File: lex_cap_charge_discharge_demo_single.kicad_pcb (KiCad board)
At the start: 2 copper layers, 38 x 33.5 mm, 8 parts, among them J1 +5V, J2 GND, SW1 charge, SW2 discharge

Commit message: Tweak R vals
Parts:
- R1: value 400K -> 10K
- R2: value 470 -> 330
- moved R1 79.5 mm to (53.0, 59.5), turned to -90 degrees
- moved R2 77.1 mm to (65.9, 53.0)
- moved SW1 73.8 mm to (52.9, 75.0)
- moved J1 70.8 mm to (53.0, 53.0)
- moved SW2 70.2 mm to (76.4, 75.0)
- moved J2 69.9 mm to (57.0, 53.0)
- moved D1 66.4 mm to (74.0, 64.0)
- moved C1 63.9 mm to (64.0, 64.0)
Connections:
- C1 pad 1: Net-(SW1-A) -> Net-(SW1-B)
- C1 pad 2: Net-(C1-Pad2) -> GND
- R1 pad 1: Net-(C1-Pad2) -> +5V
- R1 pad 2: GND -> Net-(SW1-A)
- SW1 pad 2: +5V -> Net-(SW1-B)
- SW2 pad 2: Net-(SW1-A) -> Net-(SW1-B)
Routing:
- net Net-(SW1-B): track 0.00 -> 32.0 mm
- net Net-(D1-A): track 41.2 -> 11.0 mm
- net +5V: track 28.8 -> 6.50 mm
- net Net-(D1-K): track 29.2 -> 11.2 mm
- net Net-(SW1-A): track 25.4 -> 7.93 mm
- net GND: track 30.8 -> 20.0 mm
- net Net-(C1-Pad2): track 4.88 -> 0.00 mm

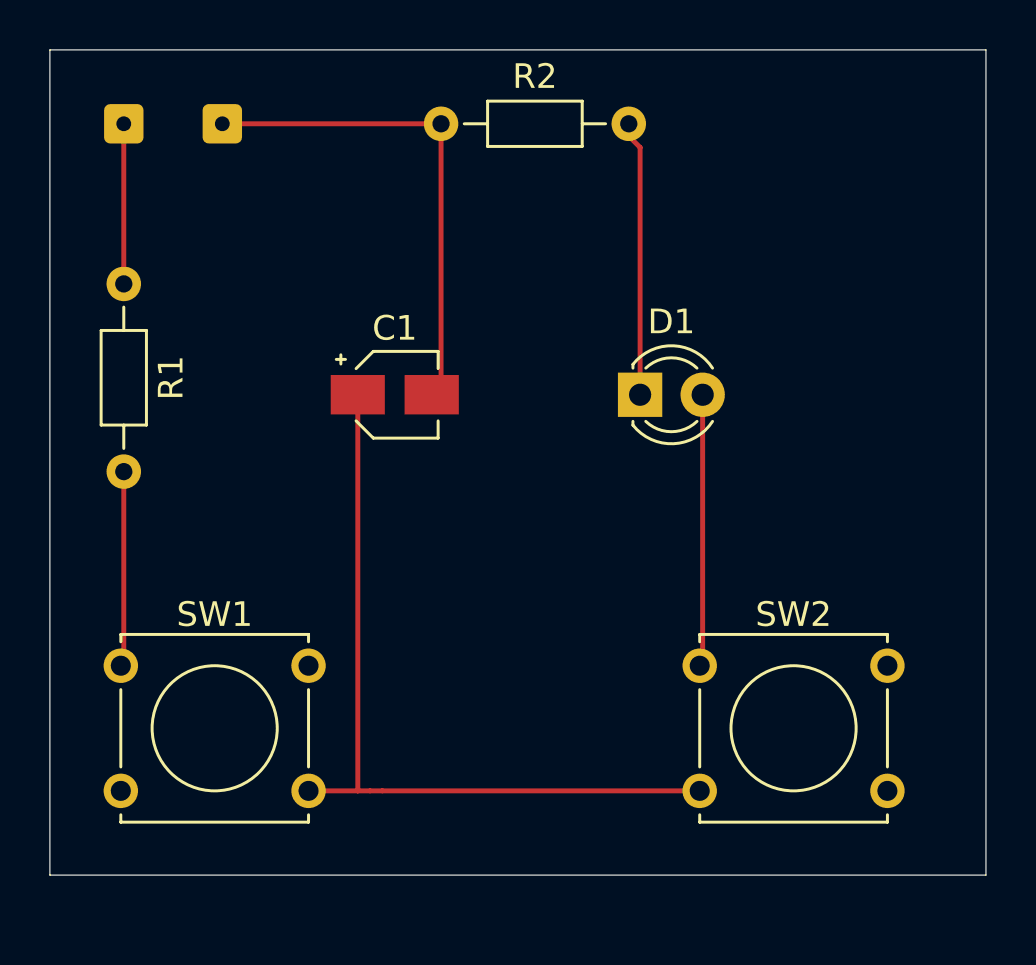
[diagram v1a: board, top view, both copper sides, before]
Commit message: Change various incl +V, GND solder pads; move components to  0.24mm standard pitch grid; add text front/back
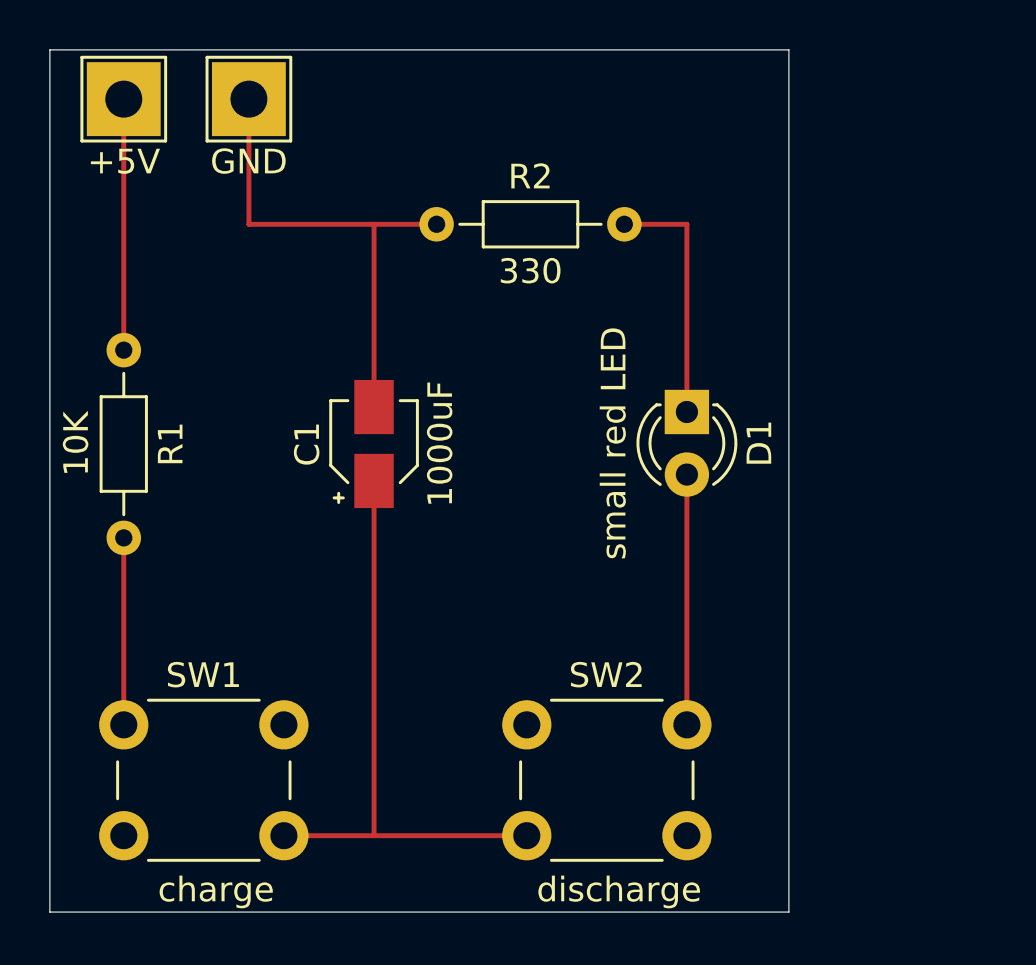
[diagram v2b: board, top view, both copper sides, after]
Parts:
- D1: value LED -> small red LED
- J1, J2: footprint Connector_Wire:SolderWire-0.1sqmm_1x01_D0.4mm_OD1mm -> TestPoint:TestPoint_THTPad_3.0x3.0mm_Drill1.5mm
- SW1, SW2: footprint Button_Switch_THT:SW_Tactile_Straight_KSL0Axx1LFTR -> Button_Switch_THT:SW_PUSH_6mm_H4.3mm
- moved SW2 7.42 mm to (69.4, 77.4)
- moved R2 4.08 mm to (65.7, 57.1)
- moved R1 2.69 mm to (53.0, 62.2)
- moved SW1 2.40 mm to (53.0, 77.4)
- moved C1 2.17 mm to (63.2, 66.0), turned to 90 degrees
- moved D1 2.02 mm to (75.9, 64.7), turned to -90 degrees
- moved J2 1.47 mm to (58.1, 52.0)
- moved J1 1.00 mm to (53.0, 52.0)
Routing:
- net Net-(SW1-B): track 32.0 -> 24.3 mm
- net +5V: track 6.50 -> 10.2 mm
- net Net-(D1-K): track 11.2 -> 10.2 mm
- net Net-(D1-A): track 11.0 -> 10.2 mm
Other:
- board size 38 x 33.5 mm -> 30 x 35 mm

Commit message: Put track across connected switch pins:
to keep kiCad ERC happy. Also more forgiving of a switch pin joint failure.
Apparently if I just ignored the warning it would be fine too.
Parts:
- J1, J2: footprint TestPoint:TestPoint_THTPad_3.0x3.0mm_Drill1.5mm -> TestPoint:TestPoint_THTPad_2.0x2.0mm_Drill1.0mm
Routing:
- net Net-(SW1-B): track 24.3 -> 37.3 mm
- net Net-(SW1-A): track 7.59 -> 14.1 mm
- net Net-(D1-A): track 10.2 -> 16.7 mm
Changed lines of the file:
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@@
 		)
 	)
-	(footprint "TestPoint:TestPoint_THTPad_3.0x3.0mm_Drill1.5mm"
+	(footprint "TestPoint:TestPoint_THTPad_2.0x2.0mm_Drill1.0mm"
 		(layer "F.Cu")
 		(at 53 52)
-		(descr "THT rectangular pad as test Point, square 3.0mm side length, hole diameter 1.5mm")
+		(descr "THT rectangular pad as test Point, square 2.0mm_Drill1.0mm  side length, hole diameter 1.0mm")
 		(tags "test point THT pad rectangle square")
 		(property "Reference" "J1"
-			(at 0 -2.398 0)
+			(at 0 -1.998 0)
 			(layer "User.1")
 			(effects
@@
 		)
 		(property "Value" "+5V"
-			(at 0 2.55 0)
+			(at 0 2.05 0)
 			(layer "F.SilkS")
 			(effects
@@
 		(attr exclude_from_pos_files)
 		(fp_line
-			(start -1.7 -1.7)
-			(end 1.7 -1.7)
-			(stroke
-				(width 0.12)
-				(type solid)
-			)
-			(layer "F.SilkS")
-		)
-		(fp_line
-			(start -1.7 1.7)
-			(end -1.7 -1.7)
-			(stroke
-				(width 0.12)
-				(type solid)
-			)
-			(layer "F.SilkS")
-		)
-		(fp_line
-			(start 1.7 -1.7)
-			(end 1.7 1.7)
-			(stroke
-				(width 0.12)
-				(type solid)
-			)
-			(layer "F.SilkS")
-		)
-		(fp_line
-			(start 1.7 1.7)
-			(end -1.7 1.7)
-			(stroke
-				(width 0.12)
-				(type solid)
-			)
-			(layer "F.SilkS")
-		)
-		(fp_line
-			(start -2 -2)
-			(end -2 2)
-			(stroke
-				(width 0.05)
-				(type solid)
-			)
-			(layer "F.CrtYd")
-		)
-		(fp_line
-			(start -2 -2)
-			(end 2 -2)
-			(stroke
-				(width 0.05)
-				(type solid)
-			)
-			(layer "F.CrtYd")
-		)
-		(fp_line
-			(start 2 2)
-			(end -2 2)
-			(stroke
-				(width 0.05)
-				(type solid)
-			)
-			(layer "F.CrtYd")
-		)
-		(fp_line
-			(start 2 2)
-			(end 2 -2)
-			(stroke
-				(width 0.05)
-				(type solid)
-			)
-			(layer "F.CrtYd")
+			(start -1.2 -1.2)
+			(end 1.2 -1.2)
+			(stroke
+				(width 0.12)
+				(type solid)
+			)
+			(layer "F.SilkS")
+		)
+		(fp_line
+			(start -1.2 1.2)
+			(end -1.2 -1.2)
+			(stroke
+				(width 0.12)
+				(type solid)
+			)
+			(layer "F.SilkS")
+		)
+		(fp_line
+			(start 1.2 -1.2)
+			(end 1.2 1.2)
+			(stroke
+				(width 0.12)
+				(type solid)
+			)
+			(layer "F.SilkS")
+		)
+		(fp_line
+			(start 1.2 1.2)
+			(end -1.2 1.2)
+			(stroke
+				(width 0.12)
+				(type solid)
+			)
+			(layer "F.SilkS")
+		)
+		(fp_line
+			(start -1.5 -1.5)
+			(end -1.5 1.5)
+			(stroke
+				(width 0.05)
+				(type solid)
+			)
+			(layer "F.CrtYd")
+		)
+		(fp_line
+			(start -1.5 -1.5)
+			(end 1.5 -1.5)
+			(stroke
+				(width 0.05)
+				(type solid)
+			)
+			(layer "F.CrtYd")
+		)
+		(fp_line
+			(start 1.5 1.5)
+			(end -1.5 1.5)
+			(stroke
+				(width 0.05)
+				(type solid)
+			)
+			(layer "F.CrtYd")
+		)
+		(fp_line
+			(start 1.5 1.5)
+			(end 1.5 -1.5)
+			(stroke
+				(width 0.05)
+				(type solid)
+			)
+			(layer "F.CrtYd")
+		)
+		(fp_text user "${REFERENCE}"
+			(at 0 -2 0)
+			(layer "User.1")
+			(effects
+				(font
+					(size 1 1)
+					(thickness 0.15)
+				)
+			)
 		)
 		(pad "1" thru_hole rect
 			(at 0 0)
-			(size 3 3)
-			(drill 1.5)
+			(size 2 2)
+			(drill 1)
 			(layers "*.Cu" "*.Mask")
 			(remove_unused_layers no)
@@
 		)
 	)
-	(footprint "TestPoint:TestPoint_THTPad_3.0x3.0mm_Drill1.5mm"
+	(footprint "TestPoint:TestPoint_THTPad_2.0x2.0mm_Drill1.0mm"
 		(layer "F.Cu")
 		(at 58.08 52)
-		(descr "THT rectangular pad as test Point, square 3.0mm side length, hole diameter 1.5mm")
+		(descr "THT rectangular pad as test Point, square 2.0mm_Drill1.0mm  side length, hole diameter 1.0mm")
 		(tags "test point THT pad rectangle square")
 		(property "Reference" "J2"
-			(at 0 -2.398 0)
+			(at 0 -1.998 0)
 			(layer "User.1")
 			(effects
@@
 		)
 		(property "Value" "GND"
-			(at 0 2.55 0)
+			(at 0 2.05 0)
 			(layer "F.SilkS")
 			(effects
@@
 		(attr exclude_from_pos_files)
 		(fp_line
-			(start -1.7 -1.7)
-			(end 1.7 -1.7)
-			(stroke
-				(width 0.12)
-				(type solid)
-			)
-			(layer "F.SilkS")
-		)
-		(fp_line
-			(start -1.7 1.7)
-			(end -1.7 -1.7)
-			(stroke
-				(width 0.12)
-				(type solid)
-			)
-			(layer "F.SilkS")
-		)
-		(fp_line
-			(start 1.7 -1.7)
-			(end 1.7 1.7)
-			(stroke
-				(width 0.12)
-				(type solid)
-			)
-			(layer "F.SilkS")
-		)
-		(fp_line
-			(start 1.7 1.7)
-			(end -1.7 1.7)
-			(stroke
-				(width 0.12)
-				(type solid)
-			)
-			(layer "F.SilkS")
-		)
-		(fp_line
-			(start -2 -2)
-			(end -2 2)
-			(stroke
-				(width 0.05)
-				(type solid)
-			)
-			(layer "F.CrtYd")
-		)
-		(fp_line
-			(start -2 -2)
-			(end 2 -2)
-			(stroke
-				(width 0.05)
-				(type solid)
-			)
-			(layer "F.CrtYd")
-		)
-		(fp_line
-			(start 2 2)
-			(end -2 2)
-			(stroke
-				(width 0.05)
-				(type solid)
-			)
-			(layer "F.CrtYd")
-		)
-		(fp_line
-			(start 2 2)
-			(end 2 -2)
-			(stroke
-				(width 0.05)
-				(type solid)
-			)
-			(layer "F.CrtYd")
+			(start -1.2 -1.2)
+			(end 1.2 -1.2)
+			(stroke
+				(width 0.12)
+				(type solid)
+			)
+			(layer "F.SilkS")
+		)
+		(fp_line
+			(start -1.2 1.2)
+			(end -1.2 -1.2)
+			(stroke
+				(width 0.12)
+				(type solid)
+			)
+			(layer "F.SilkS")
+		)
+		(fp_line
+			(start 1.2 -1.2)
+			(end 1.2 1.2)
+			(stroke
+				(width 0.12)
+				(type solid)
+			)
+			(layer "F.SilkS")
+		)
+		(fp_line
+			(start 1.2 1.2)
+			(end -1.2 1.2)
+			(stroke
+				(width 0.12)
+				(type solid)
+			)
+			(layer "F.SilkS")
+		)
+		(fp_line
+			(start -1.5 -1.5)
+			(end -1.5 1.5)
+			(stroke
+				(width 0.05)
+				(type solid)
+			)
+			(layer "F.CrtYd")
+		)
+		(fp_line
+			(start -1.5 -1.5)
+			(end 1.5 -1.5)
+			(stroke
+				(width 0.05)
+				(type solid)
+			)
+			(layer "F.CrtYd")
+		)
+		(fp_line
+			(start 1.5 1.5)
+			(end -1.5 1.5)
+			(stroke
+				(width 0.05)
+				(type solid)
+			)
+			(layer "F.CrtYd")
+		)
+		(fp_line
+			(start 1.5 1.5)
+			(end 1.5 -1.5)
+			(stroke
+				(width 0.05)
+				(type solid)
+			)
+			(layer "F.CrtYd")
+		)
+		(fp_text user "${REFERENCE}"
+			(at 0 -2 0)
+			(layer "User.1")
+			(effects
+				(font
+					(size 1 1)
+					(thickness 0.15)
+				)
+			)
 		)
 		(pad "1" thru_hole rect
 			(at 0 0)
-			(size 3 3)
-			(drill 1.5)
+			(size 2 2)
+			(drill 1)
 			(layers "*.Cu" "*.Mask")
 			(remove_unused_layers no)
@@
 	)
 	(segment
+		(start 53 77.4)
+		(end 59.5 77.4)
+		(width 0.2)
+		(layer "F.Cu")
+		(net 1)
+	)
+	(segment
 		(start 53 69.81)
 		(end 53 77.4)
@@
 		(layer "F.Cu")
 		(net 1)
+	)
+	(segment
+		(start 53 81.9)
+		(end 59.5 81.9)
+		(width 0.2)
+		(layer "F.Cu")
+		(net 2)
+	)
+	(segment
+		(start 69.36 81.9)
+		(end 75.86 81.9)
+		(width 0.2)
+		(layer "F.Cu")
+		(net 2)
 	)
 	(segment
@@
 	)
 	(segment
+		(start 69.36 77.4)
+		(end 75.86 77.4)
+		(width 0.2)
+		(layer "F.Cu")
+		(net 4)
+	)
+	(segment

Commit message: Tweak, add title
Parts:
- D1: value small red LED -> 3mm red LED
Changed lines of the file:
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@@
 		)
 		(property "Value" "discharge"
-			(at 3.75 6.7 0)
+			(at 3.14 6.7 0)
 			(layer "F.SilkS")
 			(effects
@@
 		)
 		(property "Value" "charge"
-			(at 3.75 6.7 0)
+			(at 3.2 6.7 0)
 			(layer "F.SilkS")
 			(effects
@@
 			)
 		)
-		(property "Value" "small red LED"
+		(property "Value" "3mm red LED"
 			(at 1.27 2.96 90)
 			(layer "F.SilkS")

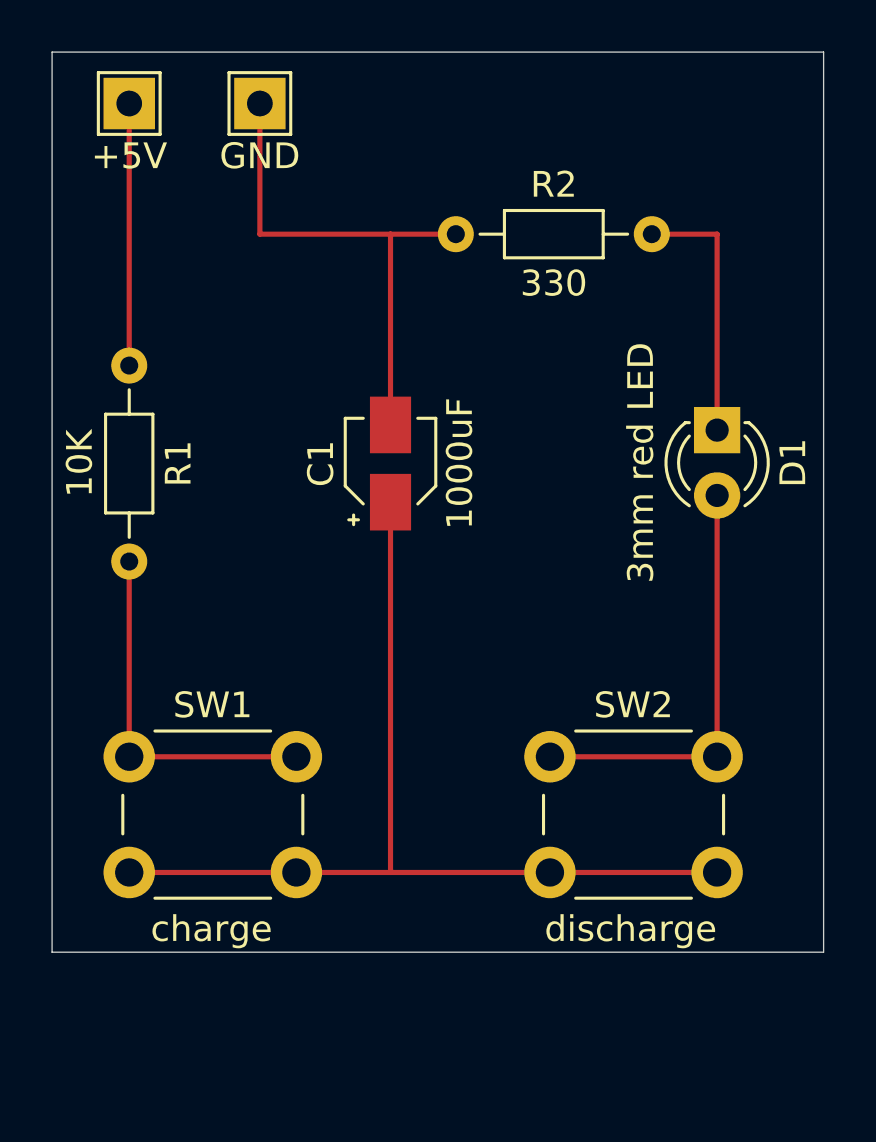
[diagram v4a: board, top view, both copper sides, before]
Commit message: Add 2.2mm mounting holes at corners (made board bigger)
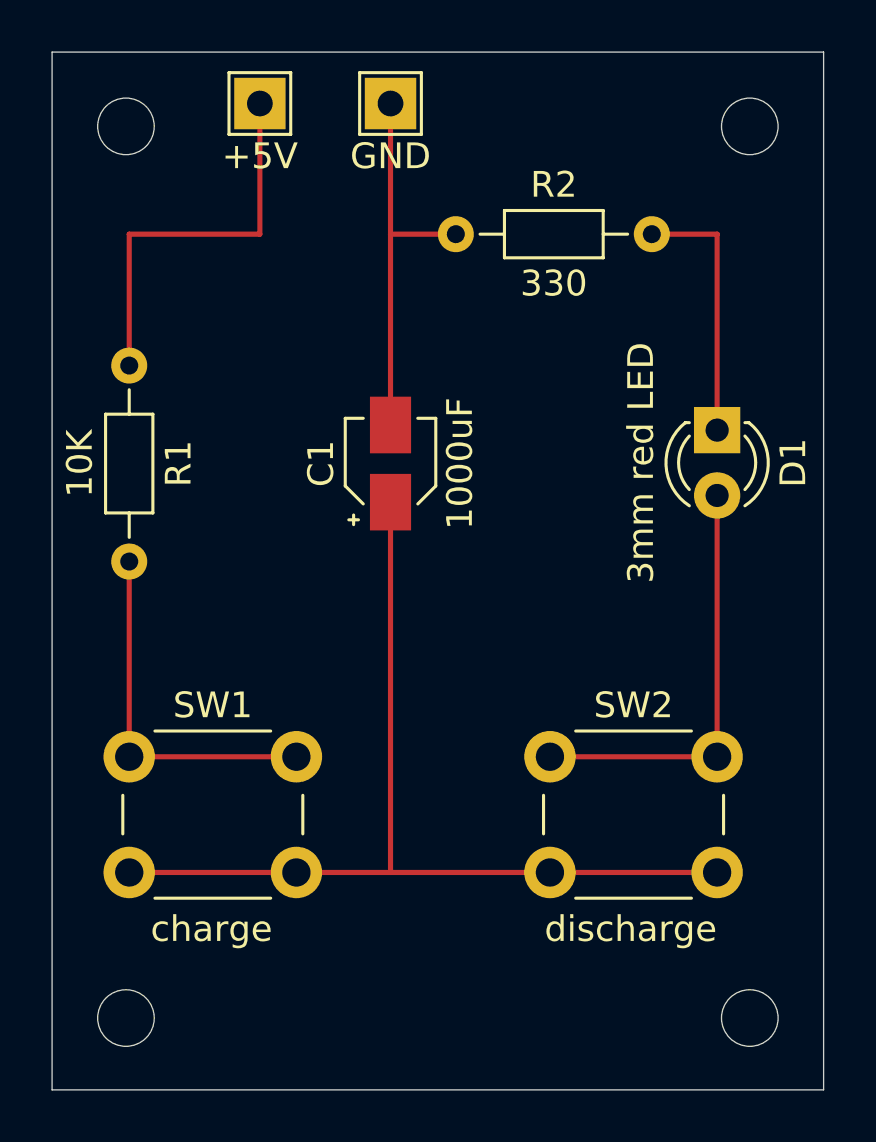
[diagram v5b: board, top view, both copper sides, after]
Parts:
- added H1: MountingHole, MountingHole:MountingHole_2.2mm_M2, F.Cu at (52.9, 87.6)
- added H2: MountingHole, MountingHole:MountingHole_2.2mm_M2, F.Cu at (77.1, 87.6)
- added H3: MountingHole, MountingHole:MountingHole_2.2mm_M2, F.Cu at (52.9, 52.9)
- added H4: MountingHole, MountingHole:MountingHole_2.2mm_M2, F.Cu at (77.1, 52.9)
- moved J1 5.08 mm to (58.1, 52.0)
- moved J2 5.08 mm to (63.2, 52.0)
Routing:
- net GND: track 20.1 -> 15.0 mm
- net +5V: track 10.2 -> 15.3 mm
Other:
- board size 30 x 35 mm -> 30 x 40.4 mm
